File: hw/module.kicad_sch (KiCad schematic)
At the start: 8 parts

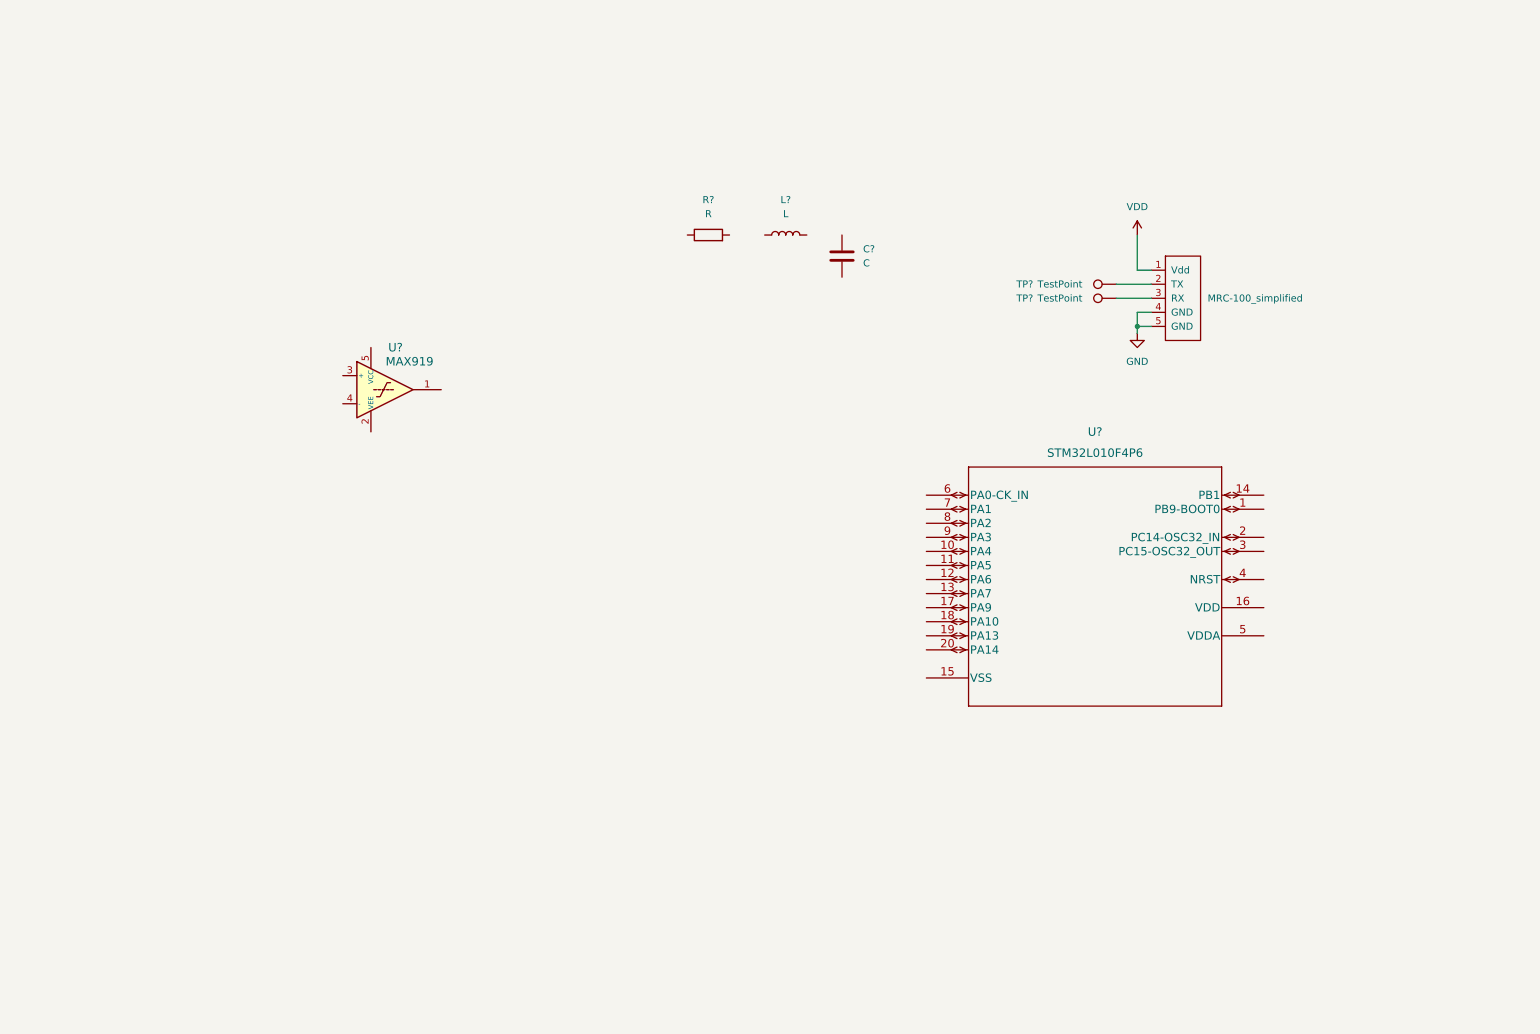
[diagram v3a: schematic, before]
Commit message: Added redundant oscillator circuit first version
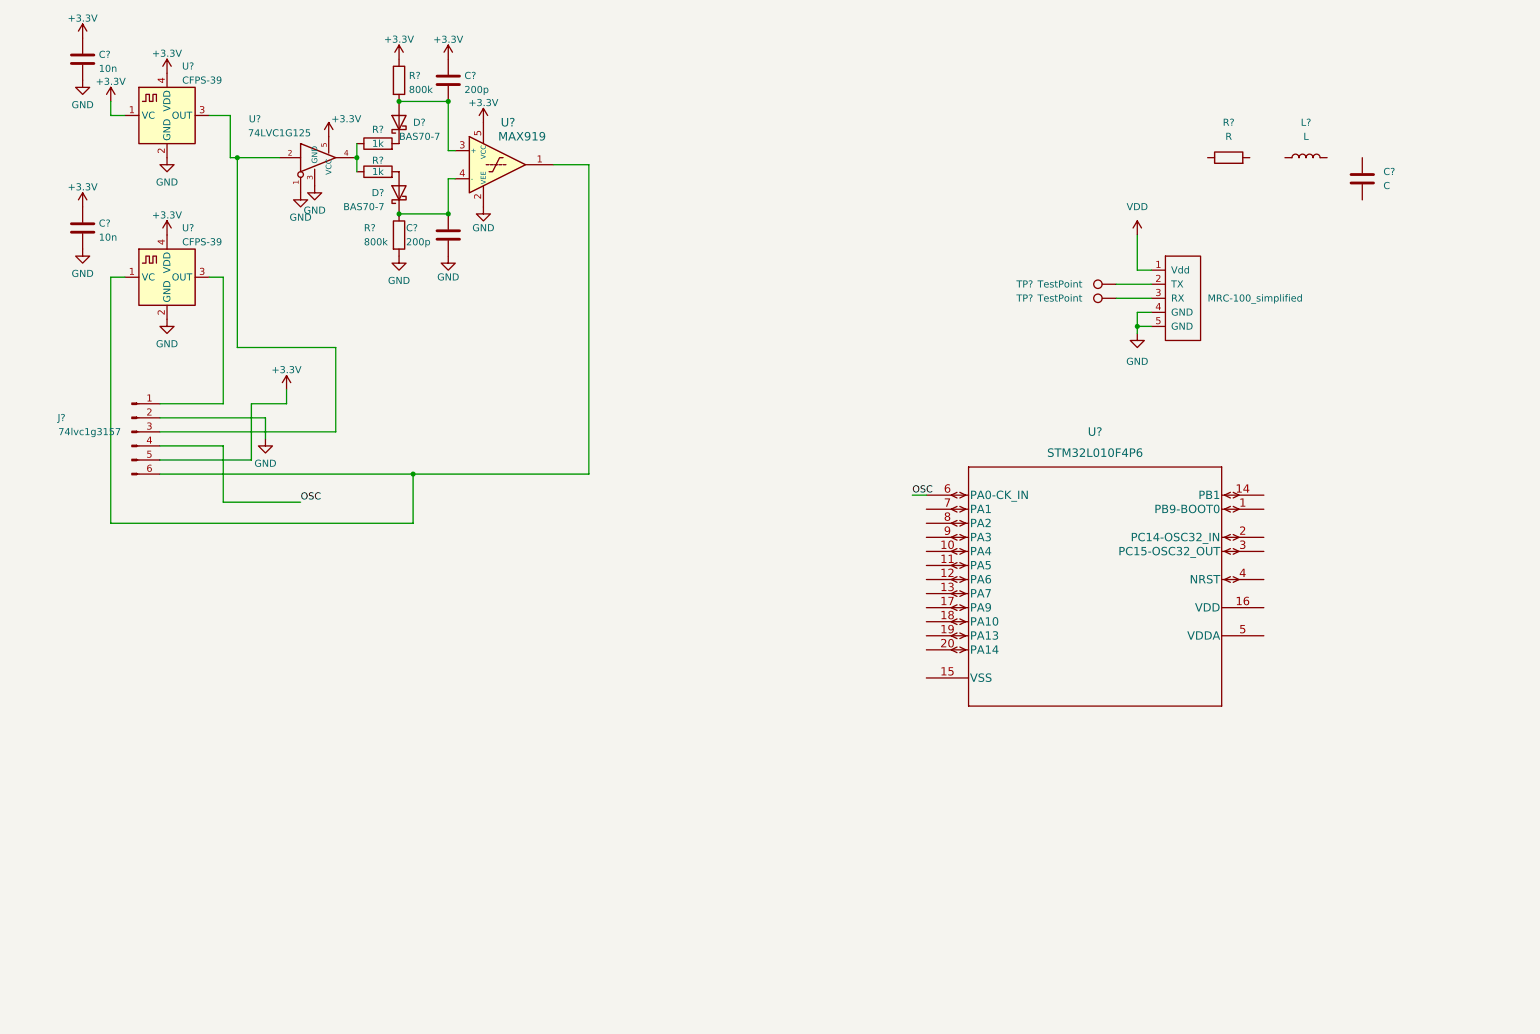
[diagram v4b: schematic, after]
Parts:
- added C? (x2): 200p, symbol Device:C
- added C? (x2): 10n, symbol Device:C
- added D? (x2): BAS70-7, symbol Device:D_Schottky
- added J?: 74lvc1g3157, symbol Connector:Conn_01x06_Male
- added R? (x2): 1k, symbol Device:R
- added R? (x2): 800k, symbol Device:R
- added U? (x2): CFPS-39, Oscillator:Oscillator_SMD_Fox_FT5H_5.0x3.2mm, symbol Oscillator:FT5HV
- added U?: 74LVC1G125, symbol 74xGxx:74LVC1G125
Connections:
- net GND: now also U?.2 (VEE), C?.2, C?.2, C?.2, J?.2 (Pin_2), R?.2, U?.1, U?.2 (GND), U?.2 (GND), U?.3 (GND)
- net OSC: now reaches U?.6 (PA0-CK_IN)
- net OSC: now also J?.4 (Pin_4)
- net at U?.1: now also J?.6 (Pin_6), U?.1 (VC)
- net at U?.3 (+): now also C?.2, D?.2 (A), R?.2
- net at U?.4 (-): now also C?.1, D?.1 (K), R?.1
- net +3.3V: now reaches U?.5 (VCC)
- net +3.3V: now also C?.1, C?.1, C?.1, J?.5 (Pin_5), R?.1, U?.1 (VC), U?.4 (VDD), U?.4 (VDD), U?.5 (VCC)
- new net: J?.3 (Pin_3), U?.2, U?.3 (OUT)
- new net: D?.1 (K), R?.2
- new net: R?.1, R?.1, U?.4
- new net: D?.2 (A), R?.2
- new net: J?.1 (Pin_1), U?.3 (OUT)
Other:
- moved on the sheet: C?, L?, R?, U?

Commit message: Placing caps, and stm pinout
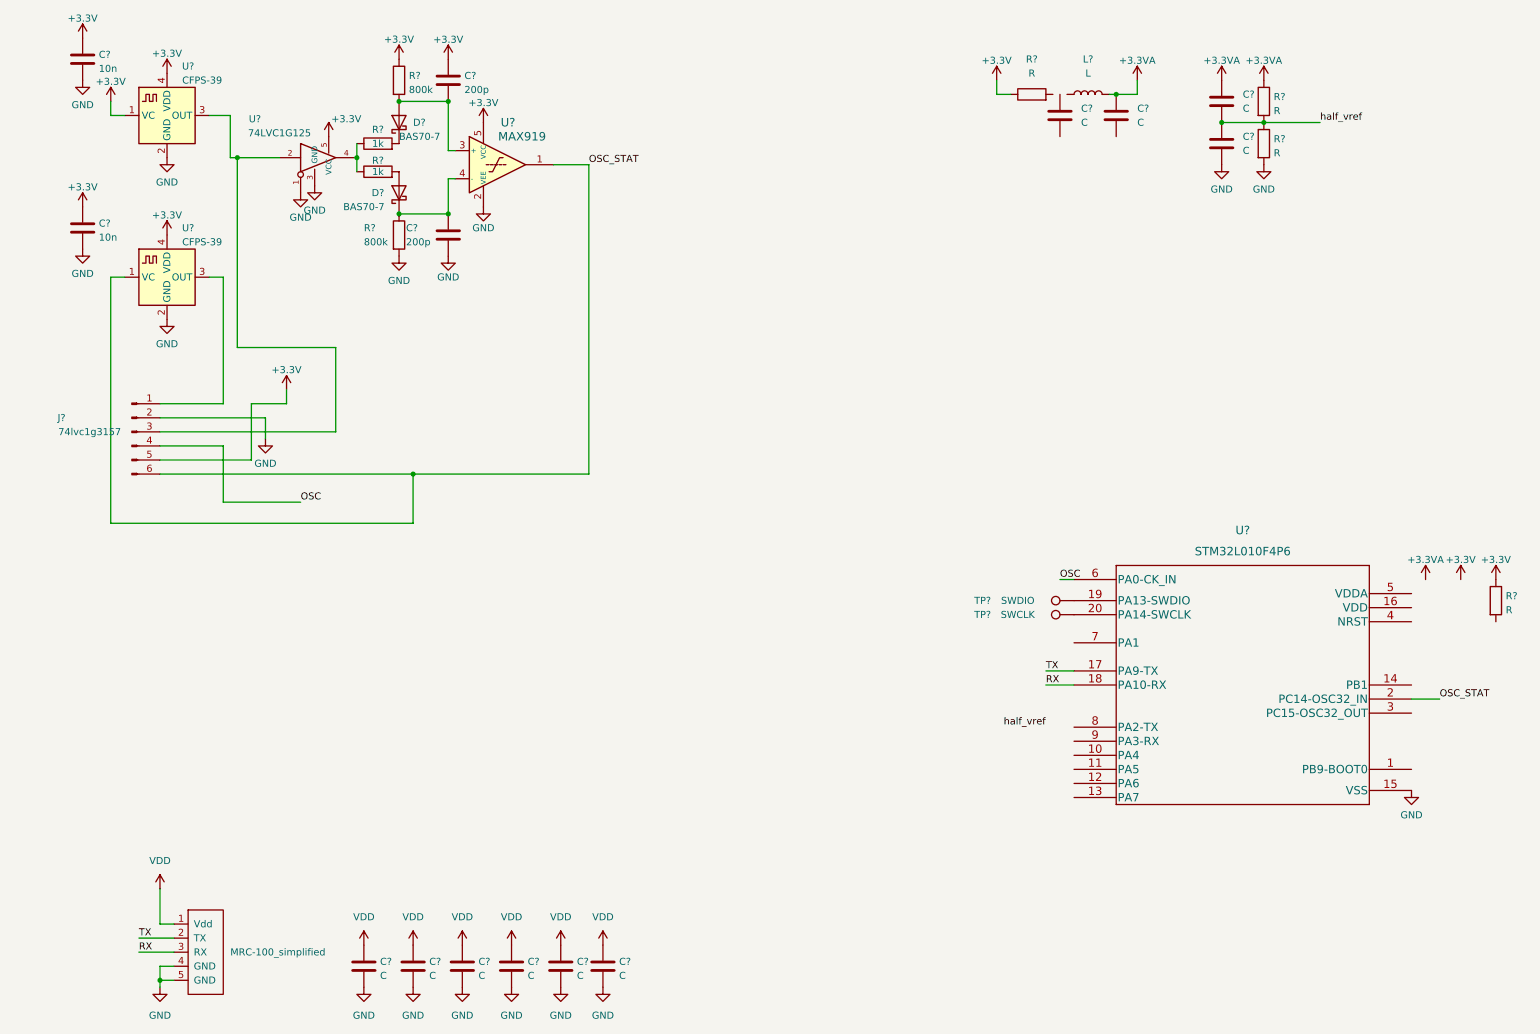
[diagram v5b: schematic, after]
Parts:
- added C? (x9): C, symbol Device:C
- added R? (x3): R, symbol Device:R
- TP?: value TestPoint -> SWCLK
- TP?: value TestPoint -> SWDIO
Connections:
- net +3.3V: now also R?.1, R?.1
- net GND: now also U?.15 (VSS), C?.2, C?.2, C?.2, C?.2, C?.2, C?.2, C?.2, R?.2
- net VDD: now also C?.1, C?.1, C?.1, C?.1, C?.1, C?.1
- net +3.3VA: now reaches L?.2
- net +3.3VA: now also C?.1, C?.1, R?.1
- net at TP?.1: now also U?.19 (PA13-SWDIO); no longer Int1.2 (TX)
- net at TP?.1: now also U?.20 (PA14-SWCLK); no longer Int1.3 (RX)
- net OSC_STAT: now reaches J?.6 (Pin_6), U?.1, U?.1 (VC)
- net OSC_STAT: now also U?.2 (PC14-OSC32_IN)
- net TX: now reaches U?.17 (PA9-TX)
- net TX: now also Int1.2 (TX)
- net RX: now reaches U?.18 (PA10-RX)
- net RX: now also Int1.3 (RX)
- new net half_vref: C?.1, C?.2, R?.1, R?.2
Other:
- moved on the sheet: C?, L?, R?, TP?

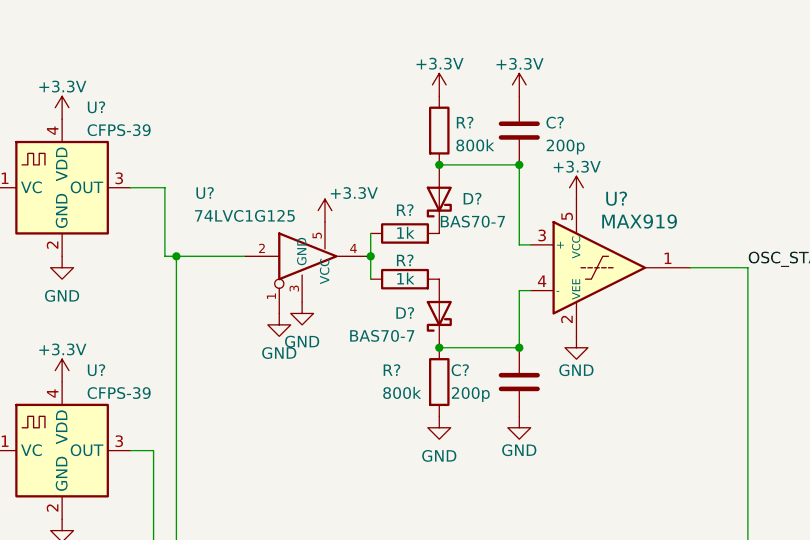
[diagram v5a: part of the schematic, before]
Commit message: Change oscillator detector resistances
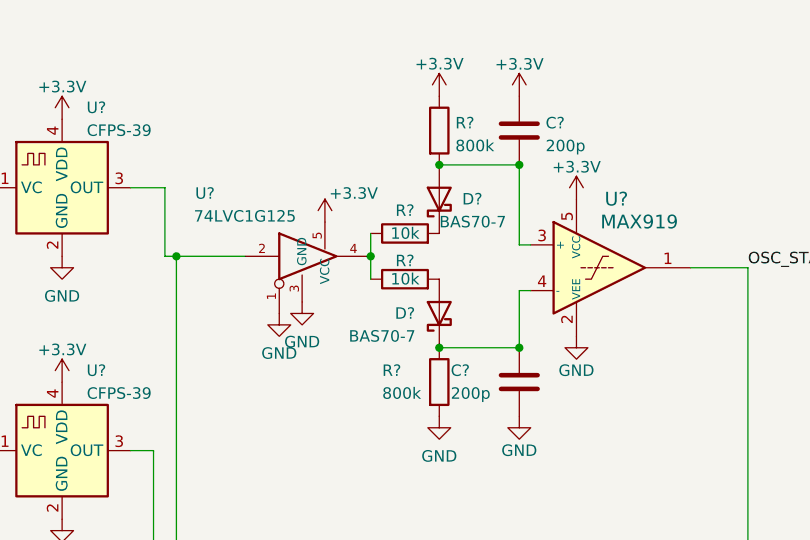
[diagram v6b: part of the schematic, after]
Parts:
- R? (x2): value 1k -> 10k
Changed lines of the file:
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@@
     (in_bom yes) (on_board yes)
     (property "Reference" "R?" (id 0) (at 71.12 39.878 90))
-    (property "Value" "1k" (id 1) (at 71.12 41.91 90))
+    (property "Value" "10k" (id 1) (at 71.12 41.91 90))
     (property "Footprint" "" (id 2) (at 71.12 43.688 90)
       (effects (font (size 1.27 1.27)) hide)
@@
     (in_bom yes) (on_board yes)
     (property "Reference" "R?" (id 0) (at 71.12 34.29 90))
-    (property "Value" "1k" (id 1) (at 71.12 36.83 90))
+    (property "Value" "10k" (id 1) (at 71.12 36.83 90))
     (property "Footprint" "" (id 2) (at 71.12 38.608 90)
       (effects (font (size 1.27 1.27)) hide)
@@
     )
     (path "/10e4a318-4512-4650-99a4-239cc5464296"
-      (reference "R?") (unit 1) (value "1k") (footprint "")
+      (reference "R?") (unit 1) (value "10k") (footprint "")
     )
     (path "/3b5914d8-e3c0-4a01-a39d-adaadd543be4"
@@
     )
     (path "/cbe05dfb-8665-406c-869c-0c5bc5b56ba7"
-      (reference "R?") (unit 1) (value "1k") (footprint "")
+      (reference "R?") (unit 1) (value "10k") (footprint "")
     )
     (path "/d5f2a7fd-4437-4a7d-8bdd-51c9f1f3e01a"

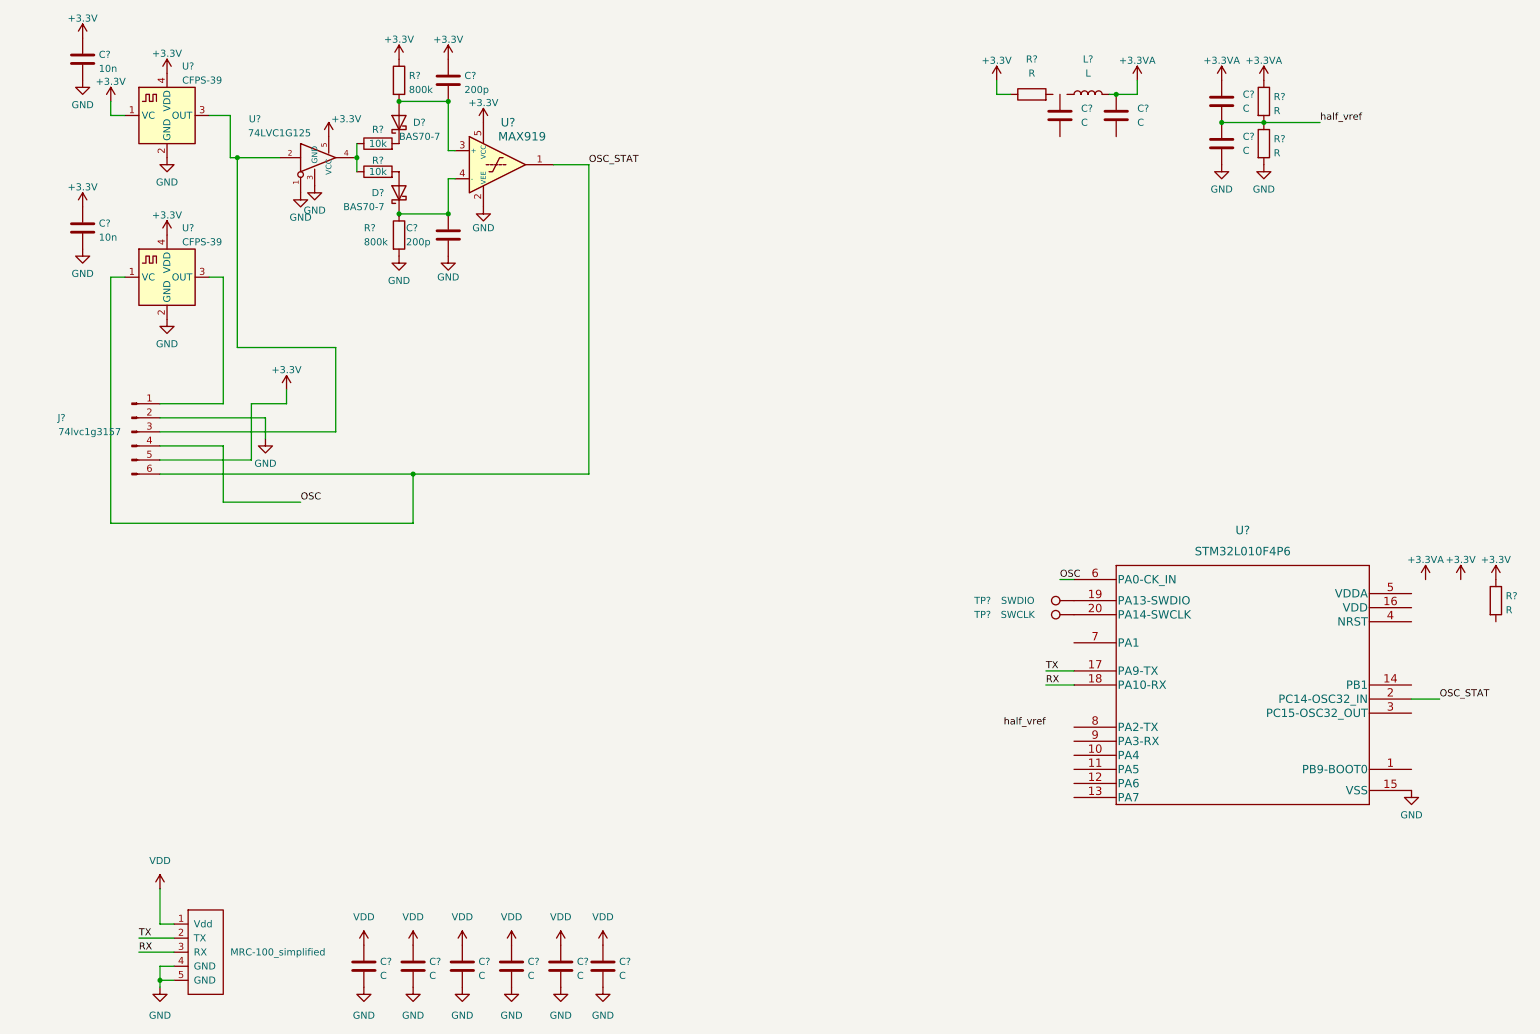
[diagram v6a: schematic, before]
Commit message: added mux
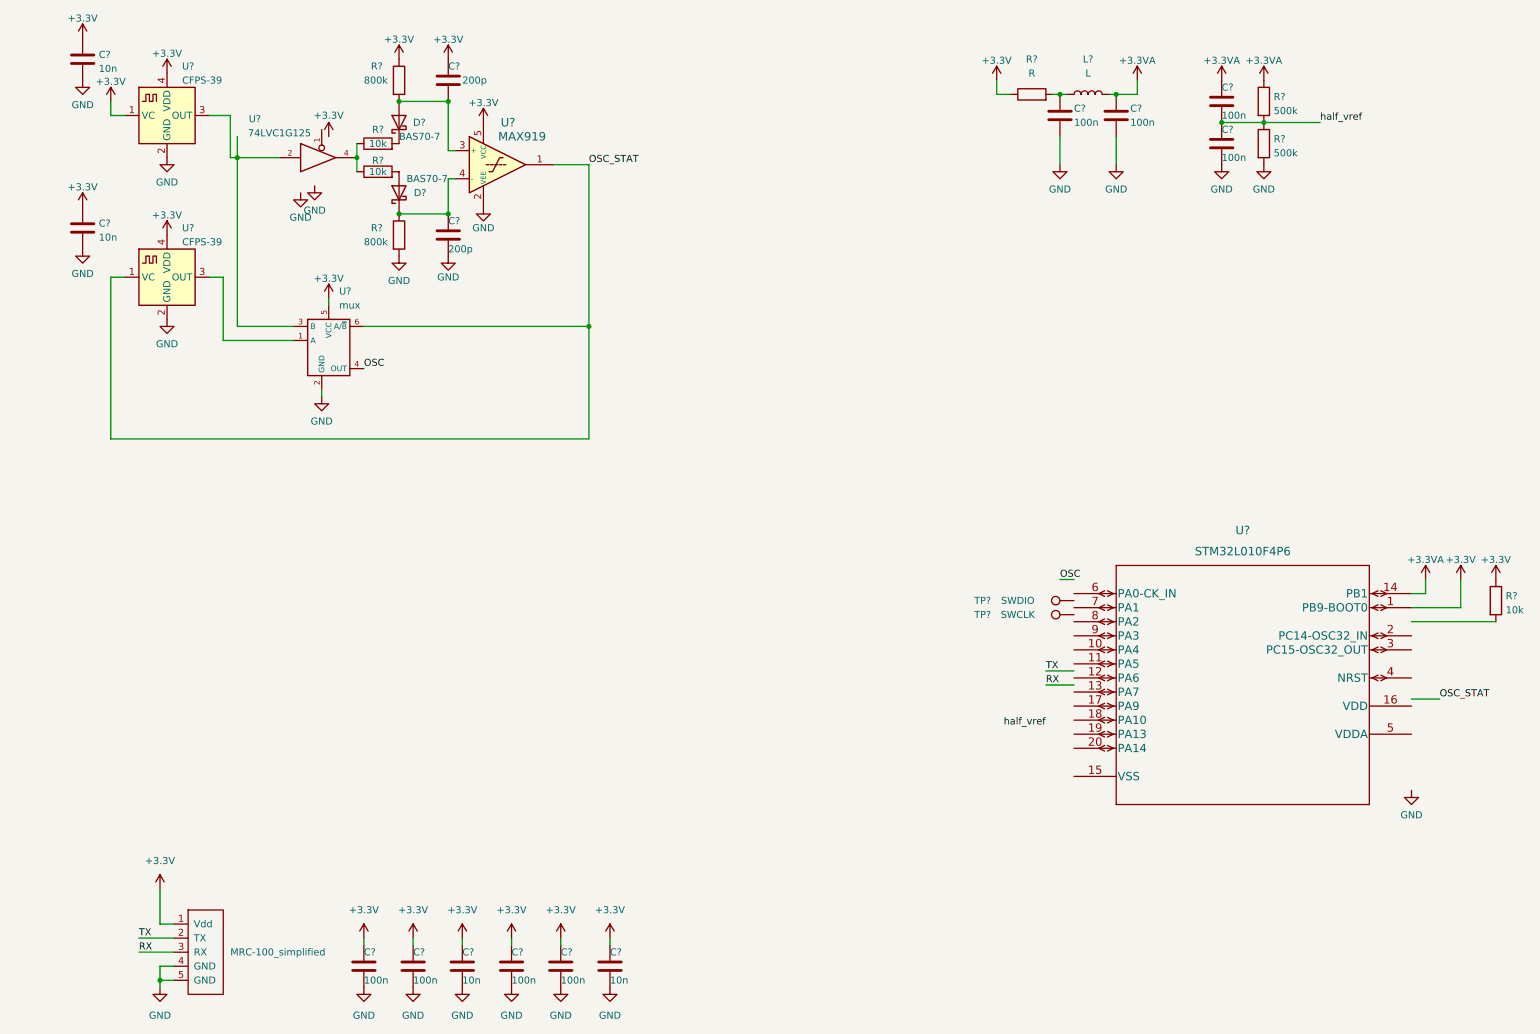
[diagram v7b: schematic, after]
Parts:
- removed J?: 74lvc1g3157, symbol Connector:Conn_01x06_Male
- added U?: mux, symbol RET:mux
- C? (x8): value C -> 100n; footprint (none) -> Capacitor_SMD:C_0805_2012Metric_Pad1.18x1.45mm_HandSolder
- C? (x4): footprint (none) -> Capacitor_SMD:C_0805_2012Metric_Pad1.18x1.45mm_HandSolder
- C? (x2): value C -> 10n; footprint (none) -> Capacitor_SMD:C_0805_2012Metric_Pad1.18x1.45mm_HandSolder
- L?: footprint (none) -> Inductor_SMD:L_0805_2012Metric_Pad1.15x1.40mm_HandSolder
- R? (x2): value R -> 500k; footprint (none) -> Resistor_SMD:R_0805_2012Metric_Pad1.20x1.40mm_HandSolder
- R? (x5): footprint (none) -> Resistor_SMD:R_0805_2012Metric_Pad1.20x1.40mm_HandSolder
- R?: value R -> 10k; footprint (none) -> Resistor_SMD:R_0805_2012Metric_Pad1.20x1.40mm_HandSolder
- U?: footprint farnell:STM32L010F4P6 -> TSSOP20
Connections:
- net VDD is gone; now on net +3.3V: C?.1, C?.1, C?.1, C?.1, C?.1, C?.1, Int1.1 (Vdd)
- net +3.3V: now also U?.1 (PB9-BOOT0), U?.5 (VCC); no longer U?.5 (VCC)
- net +3.3VA: now also U?.14 (PB1)
- net GND: now also C?.2, C?.2, U?.2 (GND); no longer U?.1, U?.15 (VSS)
- net OSC: now also U?.4 (OUT); no longer U?.6 (PA0-CK_IN)
- net OSC_STAT: now also U?.6 (A/~{B}); no longer U?.2 (PC14-OSC32_IN)
- net RX: no longer U?.18 (PA10-RX)
- net TX: no longer U?.17 (PA9-TX)
- net at U?.2, U?.3 (OUT): now also U?.3 (B)
- net at L?.1: now also C?.1, R?.2
- net at TP?.1: no longer U?.20 (PA14-SWCLK)
- net at TP?.1: no longer U?.19 (PA13-SWDIO)
- net at U?.3 (OUT): now also U?.1 (A)
- new net VCC: U?.5 (VCC)
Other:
- moved on the sheet: C?
